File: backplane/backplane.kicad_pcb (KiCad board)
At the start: 2 copper layers, 150 x 150 mm, 8 parts

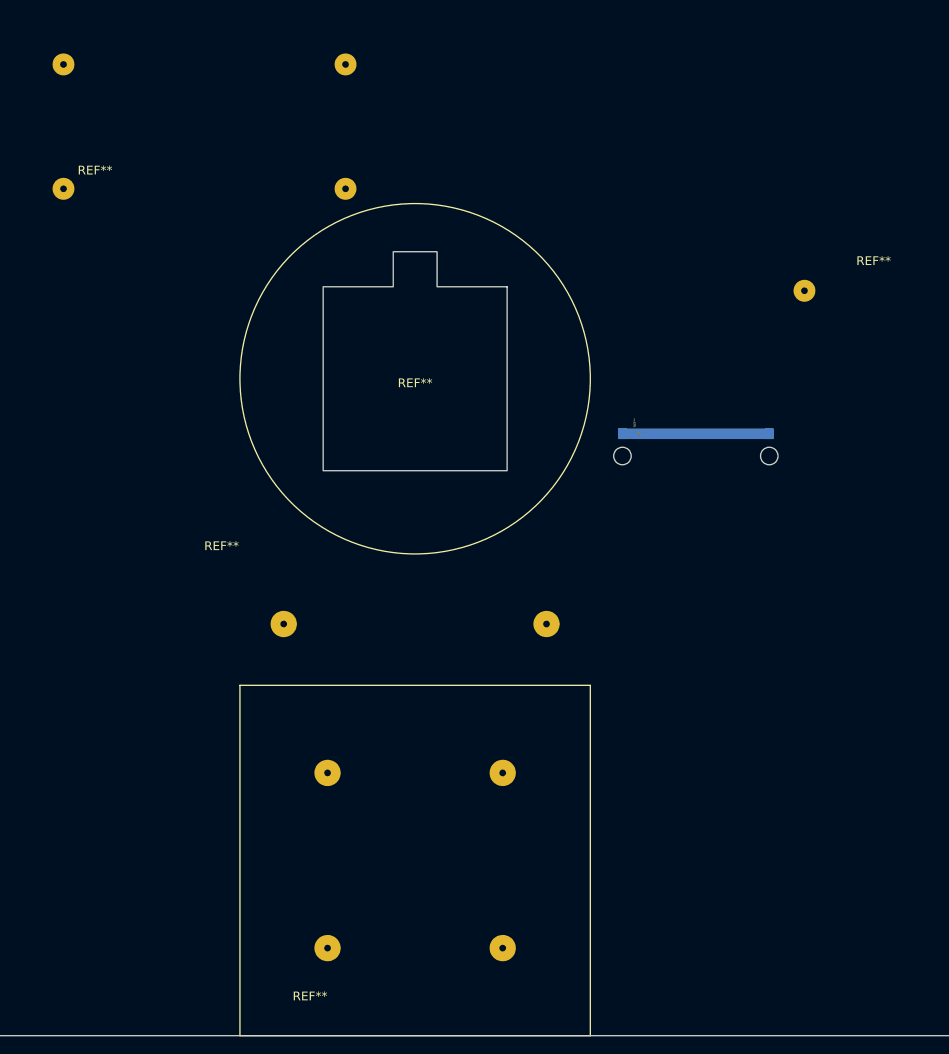
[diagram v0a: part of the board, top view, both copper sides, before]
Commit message: Updated silkscreen and REF values for footprints
Footprints now have unique names for easy reference in library.
Names for footprints have been moved around so that they don't overlap
on PCB layout.
Labels for RPi Zero connections moved outside box for visibility when
RPi is mounted onto backplane.
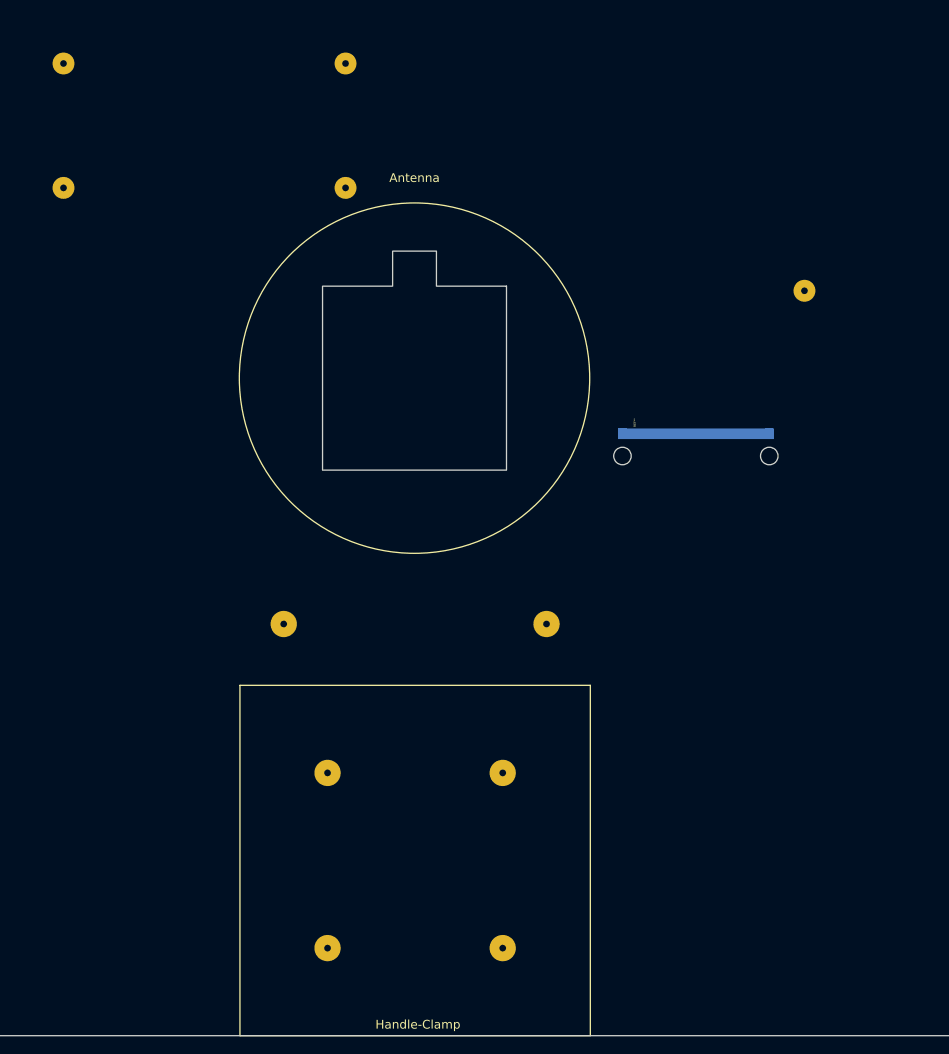
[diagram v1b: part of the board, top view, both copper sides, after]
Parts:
- removed the REF** at (56.3, 85.2)
- removed the REF** at (77.9, 180.5)
- removed the REF** at (140.2, 97.5)
- removed the REF** at (67.9, 138.5)
- removed the REF** at (97.9, 105.5)
- added Antenna: Antenna, DxWiFi:Antenna, F.Cu at (97.8, 105.4)
- added Atheros WiFi Module: Atheros WiFi Module, DxWiFi:Atheros, F.Cu at (56.3, 85.1)
- added Handle-Clamp: Handle-Clamp, DxWiFi:Handle-Clamp, F.Cu at (77.9, 180.5)
- added Phone Holder: Phone-Holder, DxWiFi:Phone-Holder, F.Cu at (67.9, 138.5)
- added Raspberry-Pi-Zero : Raspberry-Pi-Zero, DxWiFi:Raspberry-Pi-Zero, F.Cu at (140.2, 97.5)

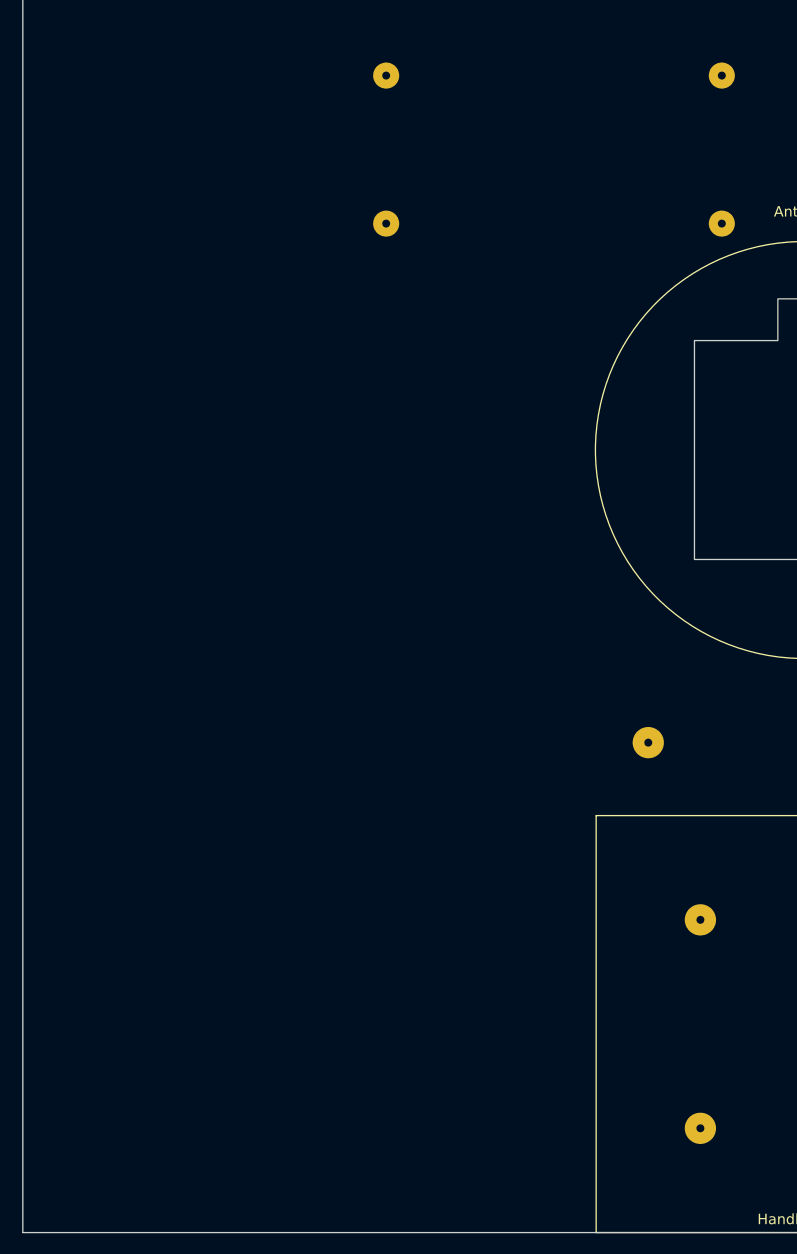
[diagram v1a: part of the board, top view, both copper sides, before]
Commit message: Added version number in silkscreen
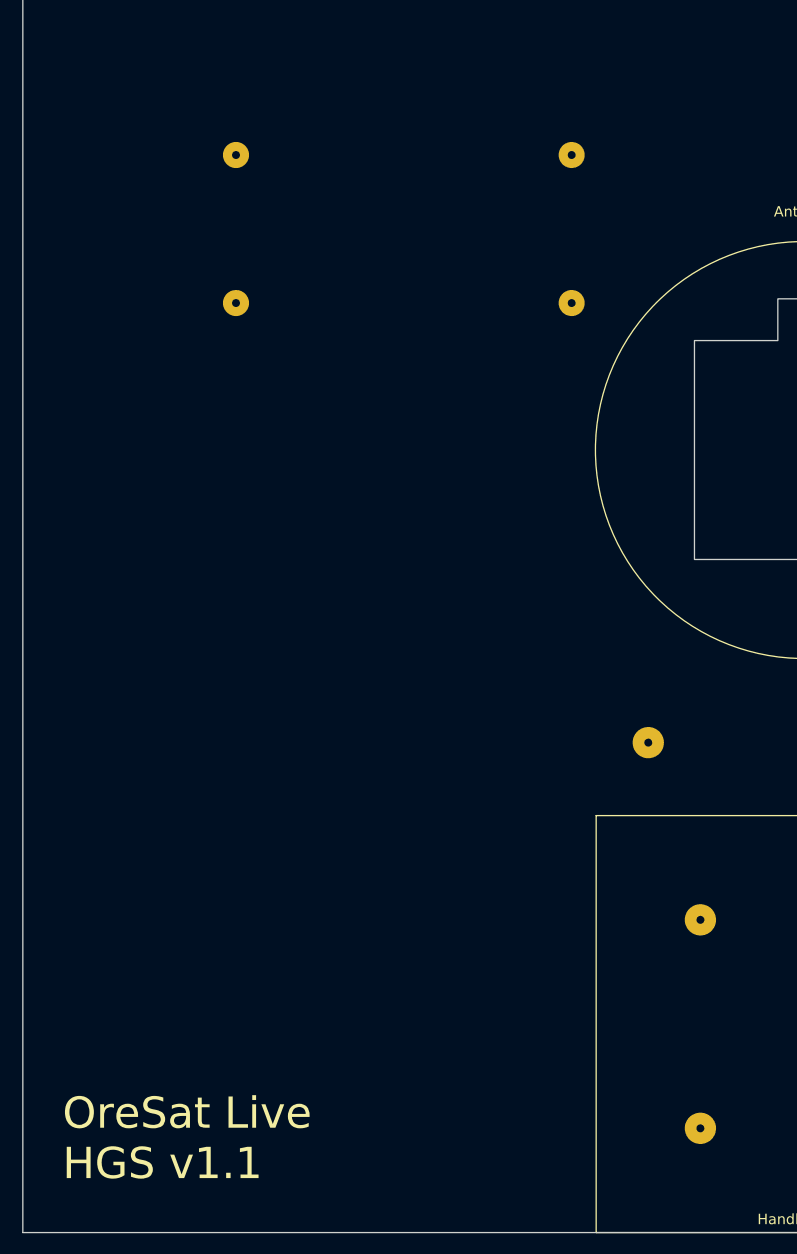
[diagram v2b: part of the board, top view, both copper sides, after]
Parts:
- moved Atheros WiFi Module 16.3 mm to (41.9, 92.7)
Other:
- board text added: "OreSat Live HGS v1.1"
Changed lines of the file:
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@@
   (general
     (thickness 1.6)
-    (drawings 4)
+    (drawings 6)
     (tracks 0)
     (zones 0)
@@
   )
   (module DxWiFi:Atheros (layer F.Cu)
-    (at 56.316 85.09)
+    (at 41.91 92.71)
     (fp_text reference "Atheros WiFi Module" (at 17.5 -3.5) (layer F.Fab) hide
       (effects (font (size 1 1) (thickness 0.15)))
@@
     (pad "" np_thru_hole circle (at 2.54 1.915 270) (size 2 2) (drill 2) (layers *.Cu *.Mask))
   )
+  (gr_text "OreSat Live\nHGS v1.1" (at 26.67 171.45) (layer F.SilkS)
+    (effects (font (size 3 3) (thickness 0.3)) (justify left))
+  )
+  (gr_text "OreSat Live\nHGS v1.1" (at 26.67 171.45) (layer B.SilkS)
+    (effects (font (size 3 3) (thickness 0.3)) (justify left))
+  )
   (gr_line (start 22.86 180.48) (end 22.86 30.48) (layer Edge.Cuts) (width 0.05))

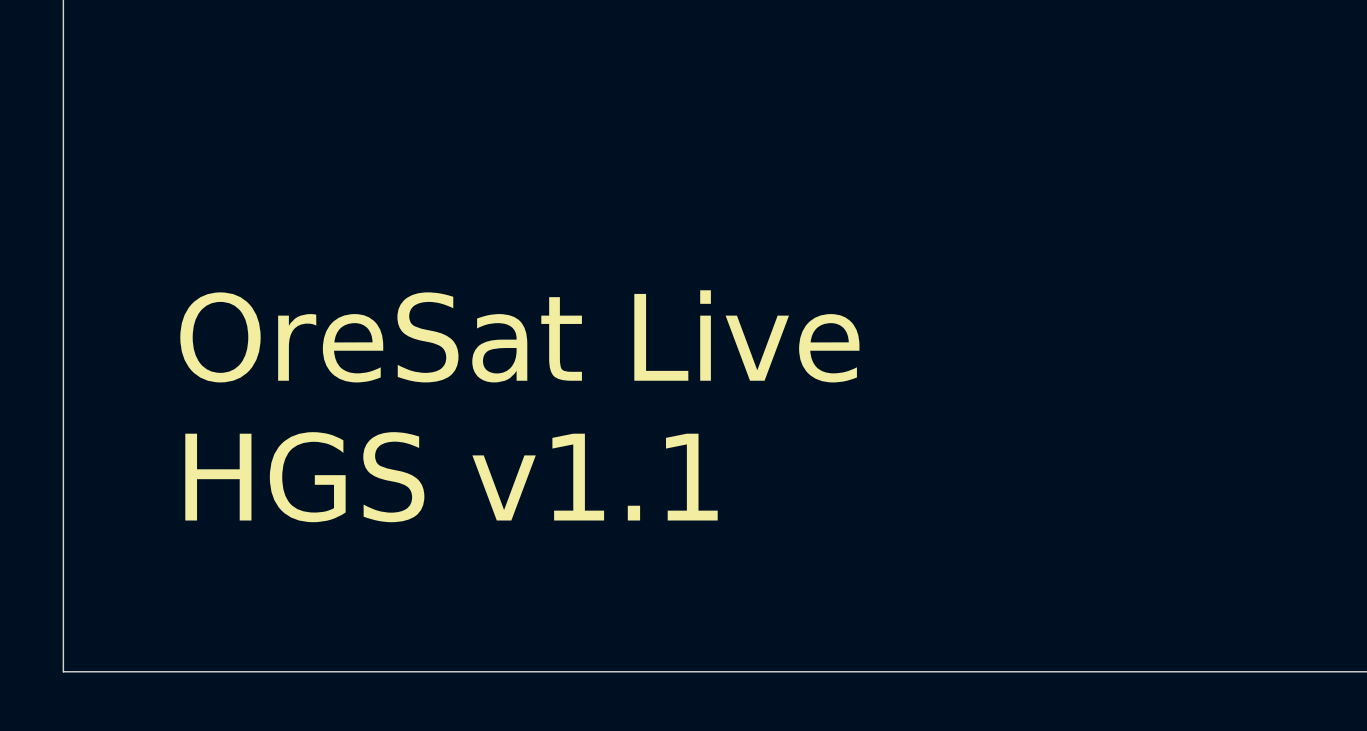
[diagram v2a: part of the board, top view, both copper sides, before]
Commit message: Added OreSat logo to silkscreen
Included dxf version of logo needed to import to Kicad
Added logo as footprint (includes version number)
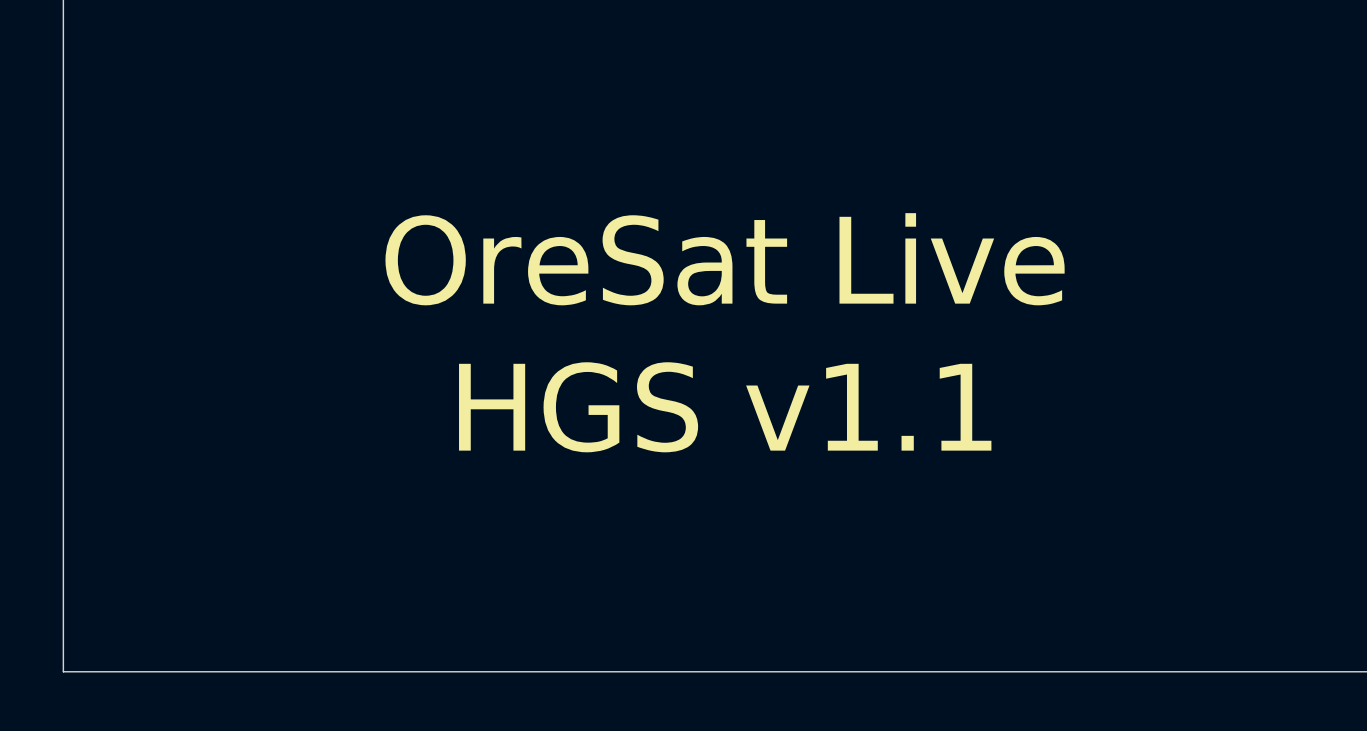
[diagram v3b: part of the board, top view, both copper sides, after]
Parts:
- added logo_oresat: logo_oresat, DxWiFi:logo_oresat, F.Cu at (45.7, 149.9)
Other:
- board text removed: "OreSat Live HGS v1.1"

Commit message: Moved logo to back silkscreen
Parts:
- moved logo_oresat 1.80 mm to (44.5, 151.1)
